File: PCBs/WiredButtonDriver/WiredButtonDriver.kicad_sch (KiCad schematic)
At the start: 35 parts, among them J6 IN, J7 OUT, Q1 AO3400A, U2 74HC164

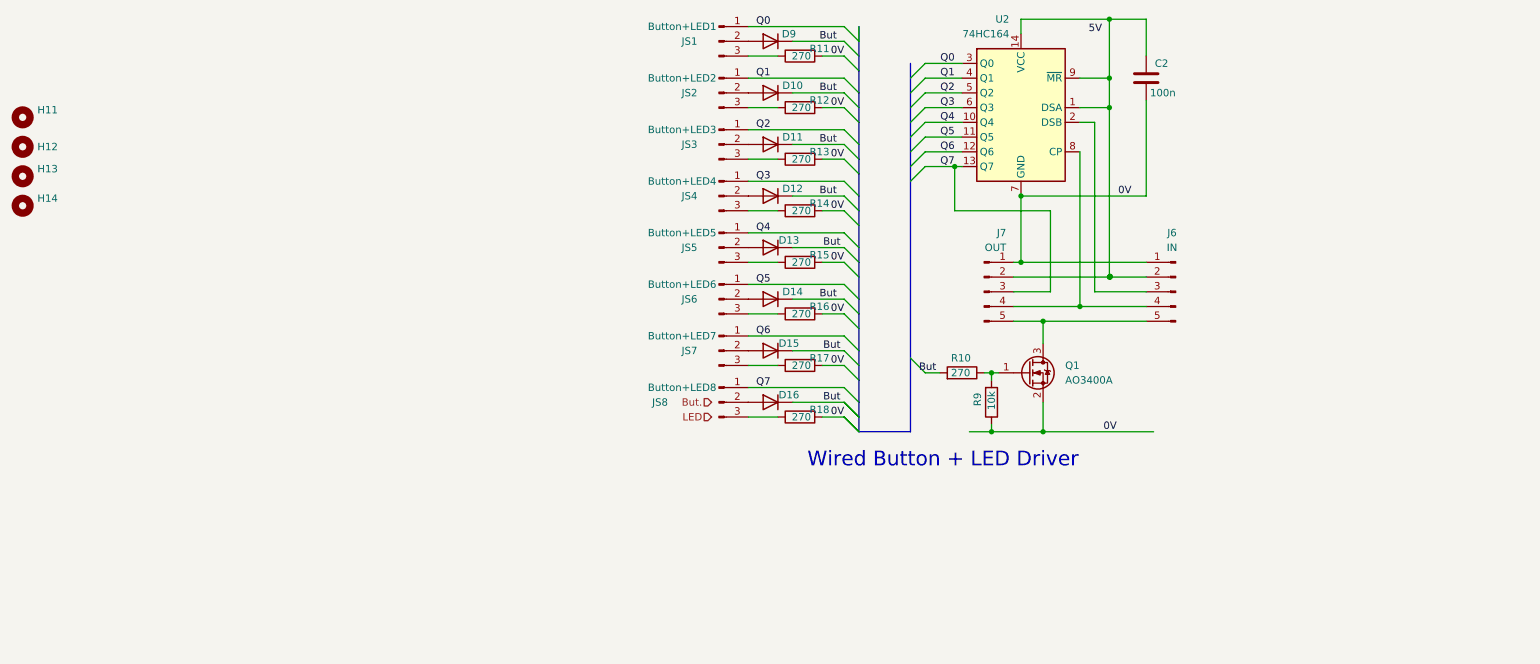
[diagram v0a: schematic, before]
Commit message: V1.1 PCB updates after initial testing 1. Share data out line between LCD, 7 Segment and button scan to yield spare io lines for    control of WS8212 LEDs for music stand lamp 2. Replace level shifting FET on Button Driver PCBs by resistor 3. Generate combined ks61,button driver & button mount prototype PCB for economic testing with JLC PCB
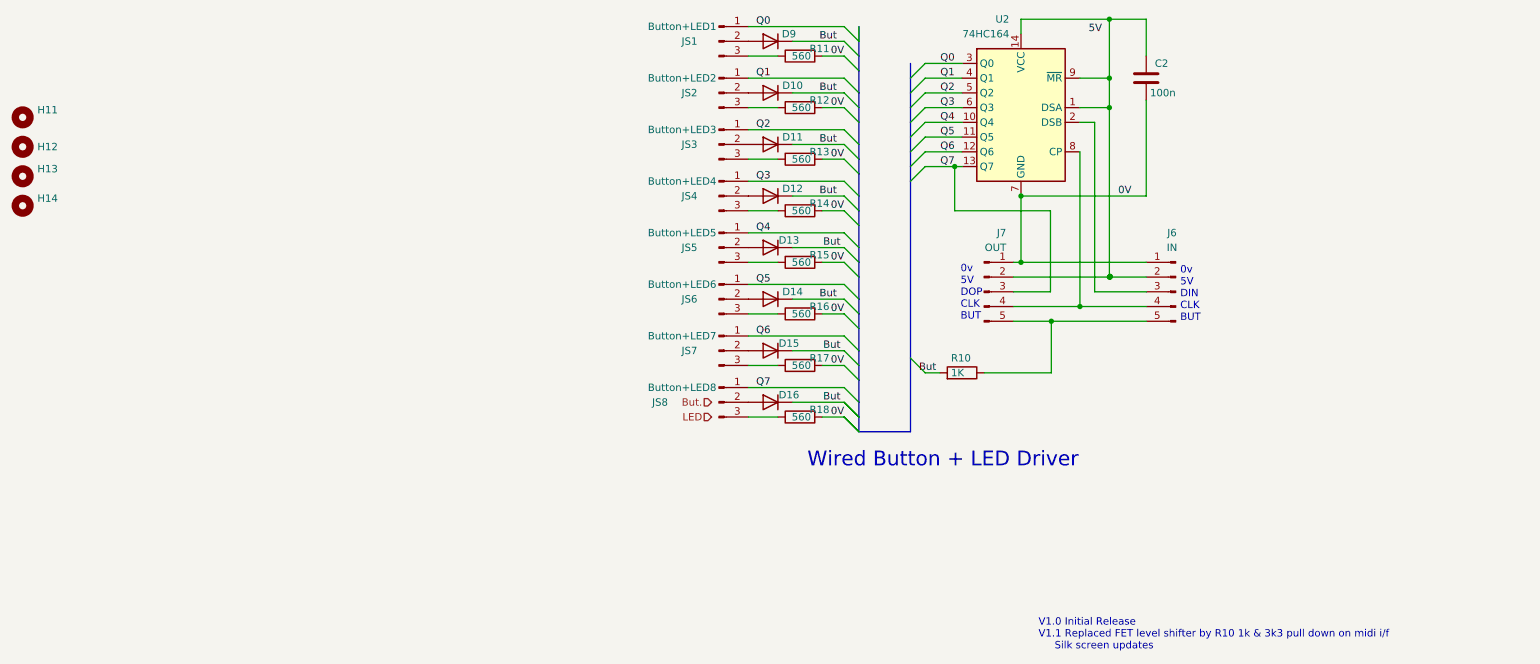
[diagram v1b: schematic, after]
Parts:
- removed Q1: AO3400A, Package_TO_SOT_SMD:SOT-23, symbol Transistor_FET:AO3400A
- removed R9: 10k, Resistor_SMD:R_0805_2012Metric_Pad1.20x1.40mm_HandSolder, symbol Device:R
- R10: value 270 -> 1K
- R11, R12, R13, R14, R15, R16, R17, R18: value 270 -> 560
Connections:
- net at R10.1: now also J6.5 (Pin_5), J7.5 (Pin_5)
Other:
- note added: "0v 5V DIN CLK BUT"
- note added: "0v 5V DOP CLK BUT"
- note added: "V1.0 Initial Release V1.1 Replaced FET level shifter by R10 1k & 3k3 pull down on midi i/f Silk screen updates"
